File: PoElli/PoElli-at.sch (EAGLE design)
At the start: 49 parts, among them J1 DF12-60DP, T1 POE-ISOLATION, U3 NCP1117, X1 RJ45MOLEX

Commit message: Added ENC624J600
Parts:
- removed U4: (no value), SparkFun-DigitalIC:ENC28J60
- added C11, C14: 10n, ELL-i-Passives:C0603
- added C12, C13: 6.8n, ELL-i-Passives:C0603
- added C15: 10u, ELL-i-Passives:C0603
- added C16: 47u, ELL-i-Passives:CPOL6032
- added C17: 100n, ELL-i-Passives:C0805
- added C18, C19: 27p, ELL-i-Passives:C0603
- added D11: GREEN, SparkFun-LED:LED-GREEN0603
- added D12: (no value), SparkFun-LED:LED-YELLOW0603
- added R16, R17: 180, ELL-i-Passives:R0402
- added R18, R20: 49.9,1%, ELL-i-Passives:R0603
- added R19: 10R, 1%, ELL-i-Passives:R0603
- added R21: 12.4k,1%, ELL-i-Passives:R0603
- added U$4: ENC624J600-I/PT, ELL-i-DigitalIC:ENC624J600-I/PT
- R1, R2: value 100 -> 49.9,1%
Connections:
- new net +3V3: C16.+, R18.1, R19.2, R2.2, U$4.VDD, U$4.VDDOSC, U$4.VDDPLL, U$4.VDDRX, U$4.VDDTX, U$4.VDD_2, U$4.VDD_3, U3.OUT, U3.TAB
- new net GNDA: C10.-, C11.2, C14.2, C15.2, C16.-, C17.2, C18.2, C19.2, D11.C, D12.C, R15.1, R21.1, U$4.A0, U$4.A1, U$4.A10, U$4.A11, U$4.A12, U$4.A13, U$4.A14/PSPCFG1, U$4.A2, U$4.A3, U$4.A4, U$4.A5, U$4.A6, U$4.A7, U$4.A8, U$4.A9, U$4.AD0, U$4.AD1, U$4.AD10, U$4.AD11, U$4.AD12, U$4.AD13, U$4.AD14, U$4.AD15, U$4.AD2, U$4.AD3, U$4.AD4, U$4.AD5, U$4.AD6, U$4.AD7, U$4.AD8, U$4.AD9, U$4.PSPCFG2, U$4.PSPCFG3, U$4.VSS, U$4.VSSOSC, U$4.VSSPLL, U$4.VSSRX, U$4.VSSTX, U$4.VSSTX1, U$4.VSS_2, U$4.WRH/B1SEL, U$7.SEC-, U3.GND
- new net N$38: D11.A, R17.1
- new net N$39: C12.1, T1.RD+
- new net N$40: C12.2, R1.1, U$4.TPIN-
- new net N$41: R16.1, U$4.LEDB
- new net N$42: R17.2, U$4.LEDA
- new net N$43: C11.1, R19.1, T1.TCT
- new net N$44: C13.2, R20.2, U$4.TPIN+
- new net N$45: R21.2, U$4.RBIAS
- new net N$46: C15.1, U$4.VCAP
- new net N$47: C19.1, U$4.OSC1
- net N$11: now also C14.1, R20.1, T1.RCT; no longer T1.RD-
- net N$12: now also C13.1, T1.RD-; no longer R1.1, T1.RD+
- net N$13: now also R18.2, U$4.TPOUT+; no longer R2.2
- net N$14: now also U$4.TPOUT-
- net N$35: now also C17.1
- net N$36: now also D12.A, R16.2; no longer C10.-, R15.1, U$7.SEC-
- net N$37: now also C18.1, U$4.OSC2; no longer U3.OUT, U3.TAB, U4.VDD, U4.VDDOSC, U4.VDDPLL, U4.VDDRX, U4.VDDTX
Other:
- moved on the sheet: J1, R1, R2, SV1, T1, U3, X1

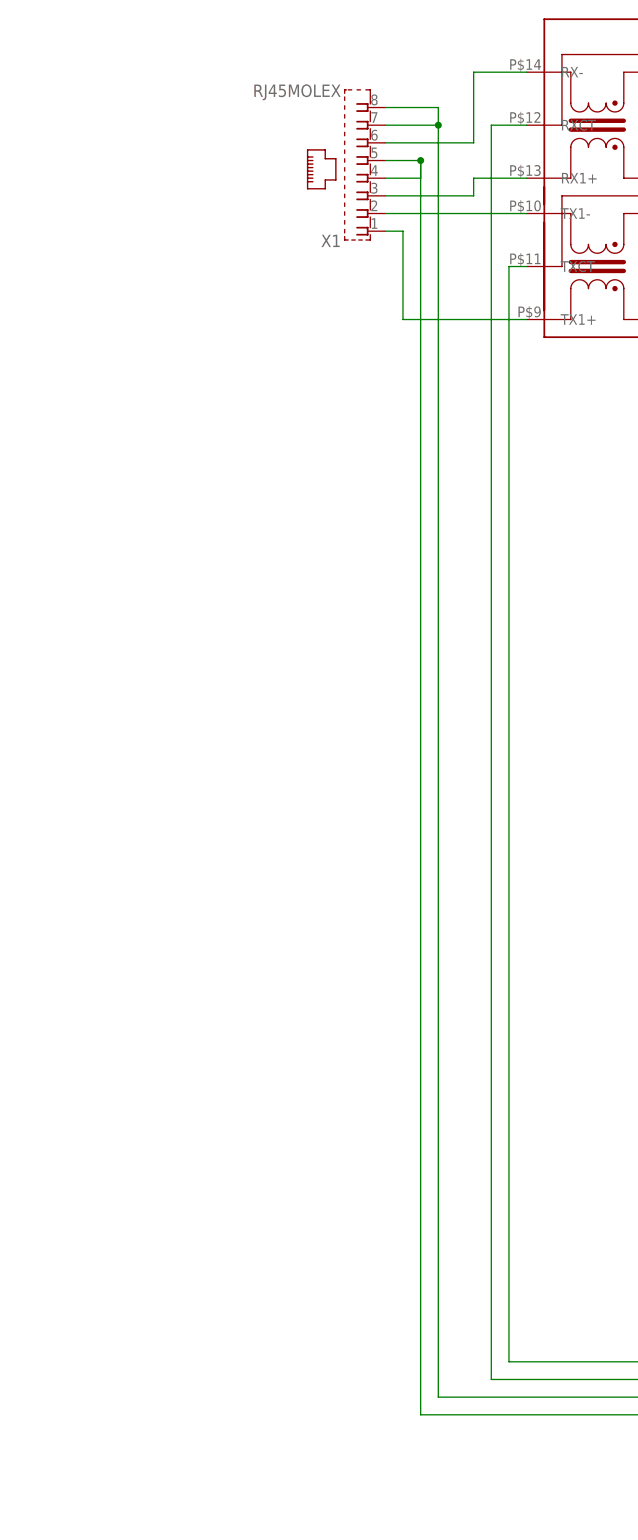
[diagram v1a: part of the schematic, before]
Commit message: Added RC-snubber to bridge rectifier
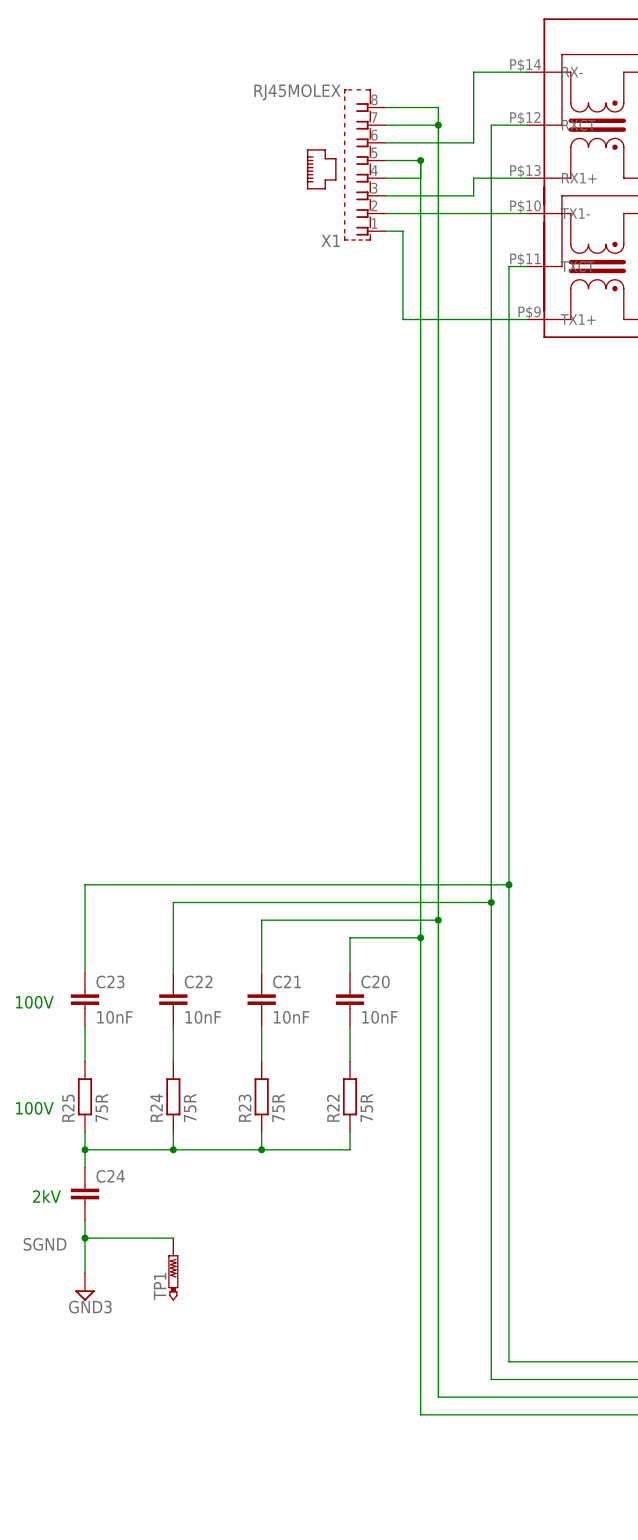
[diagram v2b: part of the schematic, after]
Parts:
- added C20, C21, C22, C23: 10nF, ELL-i-Passives:C0805
- added C24: (no value), ELL-i-Passives:C0805
- added R22, R23, R24, R25: 75R, ELL-i-Passives:R0805
- added TP1: PTR1B2,54, testpad:PTR1B2,54
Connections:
- new net N$48: C20.2, R22.2
- new net N$49: C24.1, R22.1, R23.1, R24.1, R25.1
- new net N$50: C23.2, R25.2
- new net N$51: C22.2, R24.2
- new net N$52: C21.2, R23.2
- new net SGND: C24.2, TP1.TP
- net N$10: now also C23.1
- net N$5: now also C21.1
- net N$7: now also C20.1
- net N$9: now also C22.1
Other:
- note added: "100V"
- note added: "2kV"
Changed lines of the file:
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@@
 <part name="GND15" library="supply1" deviceset="GNDA" device=""/>
 <part name="GND16" library="supply1" deviceset="GNDA" device=""/>
+<part name="R22" library="ELL-i-Passives" deviceset="R" device="0805" value="75R"/>
+<part name="R23" library="ELL-i-Passives" deviceset="R" device="0805" value="75R"/>
+<part name="R24" library="ELL-i-Passives" deviceset="R" device="0805" value="75R"/>
+<part name="R25" library="ELL-i-Passives" deviceset="R" device="0805" value="75R"/>
+<part name="C20" library="ELL-i-Passives" deviceset="C" device="0805" value="10nF"/>
+<part name="C21" library="ELL-i-Passives" deviceset="C" device="0805" value="10nF"/>
+<part name="C22" library="ELL-i-Passives" deviceset="C" device="0805" value="10nF"/>
+<part name="C23" library="ELL-i-Passives" deviceset="C" device="0805" value="10nF"/>
+<part name="C24" library="ELL-i-Passives" deviceset="C" device="0805"/>
+<part name="TP1" library="testpad" deviceset="PTR1" device="B2,54"/>
+<part name="SUPPLY1" library="supply2" deviceset="GND3" device=""/>
 </parts>
 <sheets>
 <sheet>
 <plain>
+<text x="-132.08" y="91.44" size="1.778" layer="91">2kV</text>
+<text x="-134.62" y="119.38" size="1.778" layer="91">100V</text>
+<text x="-134.62" y="104.14" size="1.778" layer="91">100V</text>
 </plain>
 <instances>
@@
 <instance part="GND15" gate="1" x="157.48" y="208.28"/>
 <instance part="GND16" gate="1" x="172.72" y="208.28"/>
+<instance part="R22" gate="G$1" x="-86.36" y="106.68" rot="R90"/>
+<instance part="R23" gate="G$1" x="-99.06" y="106.68" rot="R90"/>
+<instance part="R24" gate="G$1" x="-111.76" y="106.68" rot="R90"/>
+<instance part="R25" gate="G$1" x="-124.46" y="106.68" rot="R90"/>
+<instance part="C20" gate="G$1" x="-86.36" y="121.92"/>
+<instance part="C21" gate="G$1" x="-99.06" y="121.92"/>
+<instance part="C22" gate="G$1" x="-111.76" y="121.92"/>
+<instance part="C23" gate="G$1" x="-124.46" y="121.92"/>
+<instance part="C24" gate="G$1" x="-124.46" y="93.98"/>
+<instance part="TP1" gate="G$1" x="-111.76" y="83.82"/>
+<instance part="SUPPLY1" gate="G$1" x="-124.46" y="78.74"/>
 </instances>
 <busses>
@@
 <wire x1="-81.28" y1="248.92" x2="-73.66" y2="248.92" width="0.1524" layer="91"/>
 <wire x1="-73.66" y1="248.92" x2="-73.66" y2="246.38" width="0.1524" layer="91"/>
-<wire x1="-73.66" y1="246.38" x2="-73.66" y2="63.5" width="0.1524" layer="91"/>
+<wire x1="-73.66" y1="246.38" x2="-73.66" y2="132.08" width="0.1524" layer="91"/>
 <pinref part="X1" gate="G$1" pin="7"/>
+<wire x1="-73.66" y1="132.08" x2="-73.66" y2="63.5" width="0.1524" layer="91"/>
 <wire x1="-81.28" y1="246.38" x2="-73.66" y2="246.38" width="0.1524" layer="91"/>
 <junction x="-73.66" y="246.38"/>
@@
 <wire x1="-5.08" y1="63.5" x2="-73.66" y2="63.5" width="0.1524" layer="91"/>
 <junction x="-5.08" y="63.5"/>
+<pinref part="C21" gate="G$1" pin="1"/>
+<wire x1="-99.06" y1="124.46" x2="-99.06" y2="132.08" width="0.1524" layer="91"/>
+<wire x1="-99.06" y1="132.08" x2="-73.66" y2="132.08" width="0.1524" layer="91"/>
+<junction x="-73.66" y="132.08"/>
 </segment>
 </net>
@@
 <wire x1="-15.24" y1="68.58" x2="-15.24" y2="43.18" width="0.1524" layer="91"/>
 <wire x1="-60.96" y1="226.06" x2="-63.5" y2="226.06" width="0.1524" layer="91"/>
-<wire x1="-63.5" y1="226.06" x2="-63.5" y2="68.58" width="0.1524" layer="91"/>
+<wire x1="-63.5" y1="226.06" x2="-63.5" y2="137.16" width="0.1524" layer="91"/>
+<junction x="-15.24" y="68.58"/>
+<wire x1="-63.5" y1="137.16" x2="-63.5" y2="68.58" width="0.1524" layer="91"/>
 <wire x1="-15.24" y1="68.58" x2="-63.5" y2="68.58" width="0.1524" layer="91"/>
-<junction x="-15.24" y="68.58"/>
+<pinref part="C23" gate="G$1" pin="1"/>
+<wire x1="-124.46" y1="124.46" x2="-124.46" y2="137.16" width="0.1524" layer="91"/>
+<wire x1="-124.46" y1="137.16" x2="-63.5" y2="137.16" width="0.1524" layer="91"/>
+<junction x="-63.5" y="137.16"/>
 </segment>
 </net>
@@
 <wire x1="-10.16" y1="66.04" x2="-10.16" y2="43.18" width="0.1524" layer="91"/>
 <wire x1="-60.96" y1="246.38" x2="-66.04" y2="246.38" width="0.1524" layer="91"/>
-<wire x1="-66.04" y1="246.38" x2="-66.04" y2="66.04" width="0.1524" layer="91"/>
+<wire x1="-66.04" y1="246.38" x2="-66.04" y2="134.62" width="0.1524" layer="91"/>
+<wire x1="-66.04" y1="134.62" x2="-66.04" y2="66.04" width="0.1524" layer="91"/>
 <wire x1="-10.16" y1="66.04" x2="-66.04" y2="66.04" width="0.1524" layer="91"/>
 <junction x="-10.16" y="66.04"/>
+<pinref part="C22" gate="G$1" pin="1"/>
+<wire x1="-111.76" y1="124.46" x2="-111.76" y2="134.62" width="0.1524" layer="91"/>
+<wire x1="-111.76" y1="134.62" x2="-66.04" y2="134.62" width="0.1524" layer="91"/>
+<junction x="-66.04" y="134.62"/>
 </segment>
 </net>
@@
 <pinref part="X1" gate="G$1" pin="5"/>
 <wire x1="-81.28" y1="241.3" x2="-76.2" y2="241.3" width="0.1524" layer="91"/>
-<wire x1="-76.2" y1="241.3" x2="-76.2" y2="60.96" width="0.1524" layer="91"/>
+<wire x1="-76.2" y1="241.3" x2="-76.2" y2="129.54" width="0.1524" layer="91"/>
 <pinref part="X1" gate="G$1" pin="4"/>
+<wire x1="-76.2" y1="129.54" x2="-76.2" y2="60.96" width="0.1524" layer="91"/>
 <wire x1="-81.28" y1="238.76" x2="-76.2" y2="238.76" width="0.1524" layer="91"/>
 <wire x1="-76.2" y1="238.76" x2="-76.2" y2="241.3" width="0.1524" layer="91"/>
 <junction x="-76.2" y="241.3"/>
+<pinref part="C20" gate="G$1" pin="1"/>
+<wire x1="-86.36" y1="124.46" x2="-86.36" y2="129.54" width="0.1524" layer="91"/>
+<wire x1="-86.36" y1="129.54" x2="-76.2" y2="129.54" width="0.1524" layer="91"/>
+<junction x="-76.2" y="129.54"/>
 </segment>
 </net>
@@
 </segment>
 </net>
+<net name="N$49" class="0">
+<segment>
+<pinref part="C24" gate="G$1" pin="1"/>
+<wire x1="-124.46" y1="99.06" x2="-124.46" y2="96.52" width="0.1524" layer="91"/>
+<wire x1="-86.36" y1="99.06" x2="-99.06" y2="99.06" width="0.1524" layer="91"/>
+<pinref part="R25" gate="G$1" pin="1"/>
+<wire x1="-99.06" y1="99.06" x2="-111.76" y2="99.06" width="0.1524" layer="91"/>
+<wire x1="-111.76" y1="99.06" x2="-124.46" y2="99.06" width="0.1524" layer="91"/>
+<wire x1="-124.46" y1="99.06" x2="-124.46" y2="101.6" width="0.1524" layer="91"/>
+<pinref part="R24" gate="G$1" pin="1"/>
+<wire x1="-111.76" y1="101.6" x2="-111.76" y2="99.06" width="0.1524" layer="91"/>
+<pinref part="R23" gate="G$1" pin="1"/>
+<wire x1="-99.06" y1="101.6" x2="-99.06" y2="99.06" width="0.1524" layer="91"/>
+<pinref part="R22" gate="G$1" pin="1"/>
+<wire x1="-86.36" y1="101.6" x2="-86.36" y2="99.06" width="0.1524" layer="91"/>
+<junction x="-124.46" y="99.06"/>
+<junction x="-111.76" y="99.06"/>
+<junction x="-99.06" y="99.06"/>
+</segment>
+</net>
+<net name="SGND" class="0">
+<segment>
+<pinref part="SUPPLY1" gate="G$1" pin="GND3"/>
+<pinref part="C24" gate="G$1" pin="2"/>
+<wire x1="-124.46" y1="81.28" x2="-124.46" y2="86.36" width="0.1524" layer="91"/>
+<pinref part="TP1" gate="G$1" pin="TP"/>
+<wire x1="-124.46" y1="86.36" x2="-124.46" y2="88.9" width="0.1524" layer="91"/>
+<wire x1="-111.76" y1="86.36" x2="-124.46" y2="86.36" width="0.1524" layer="91"/>
+<junction x="-124.46" y="86.36"/>
+<label x="-127" y="86.36" size="1.778" layer="95" rot="R180"/>
+</segment>
+</net>
+<net name="N$48" class="0">
+<segment>
+<pinref part="R22" gate="G$1" pin="2"/>
+<pinref part="C20" gate="G$1" pin="2"/>
+<wire x1="-86.36" y1="111.76" x2="-86.36" y2="116.84" width="0.1524" layer="91"/>
+</segment>
+</net>
+<net name="N$50" class="0">
+<segment>
+<pinref part="C23" gate="G$1" pin="2"/>
+<pinref part="R25" gate="G$1" pin="2"/>
+<wire x1="-124.46" y1="116.84" x2="-124.46" y2="111.76" width="0.1524" layer="91"/>
+</segment>
+</net>
+<net name="N$51" class="0">
+<segment>
+<pinref part="R24" gate="G$1" pin="2"/>
+<pinref part="C22" gate="G$1" pin="2"/>
+<wire x1="-111.76" y1="111.76" x2="-111.76" y2="116.84" width="0.1524" layer="91"/>
+</segment>
+</net>
+<net name="N$52" class="0">
+<segment>
+<pinref part="C21" gate="G$1" pin="2"/>
+<pinref part="R23" gate="G$1" pin="2"/>
+<wire x1="-99.06" y1="116.84" x2="-99.06" y2="111.76" width="0.1524" layer="91"/>
+</segment>
+</net>

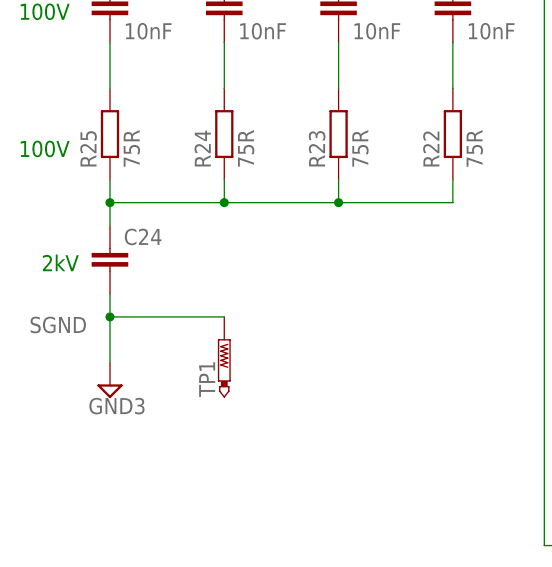
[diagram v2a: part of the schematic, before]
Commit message: Added RC-snubber value
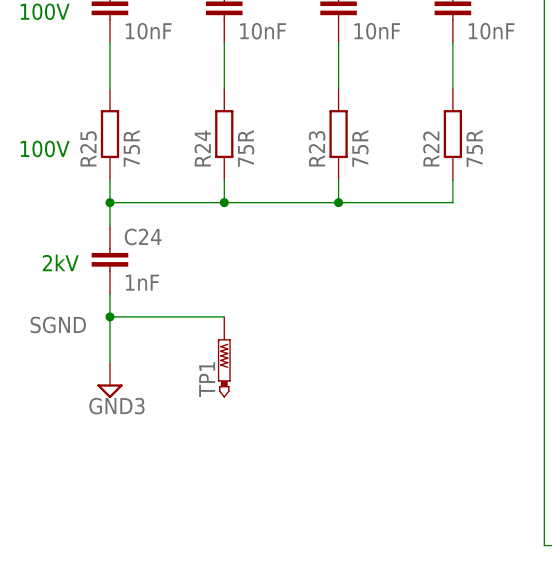
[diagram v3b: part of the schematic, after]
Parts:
- C24: value (none) -> 1nF
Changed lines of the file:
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@@
 <part name="C22" library="ELL-i-Passives" deviceset="C" device="0805" value="10nF"/>
 <part name="C23" library="ELL-i-Passives" deviceset="C" device="0805" value="10nF"/>
-<part name="C24" library="ELL-i-Passives" deviceset="C" device="0805"/>
+<part name="C24" library="ELL-i-Passives" deviceset="C" device="0805" value="1nF"/>
 <part name="TP1" library="testpad" deviceset="PTR1" device="B2,54"/>
 <part name="SUPPLY1" library="supply2" deviceset="GND3" device=""/>

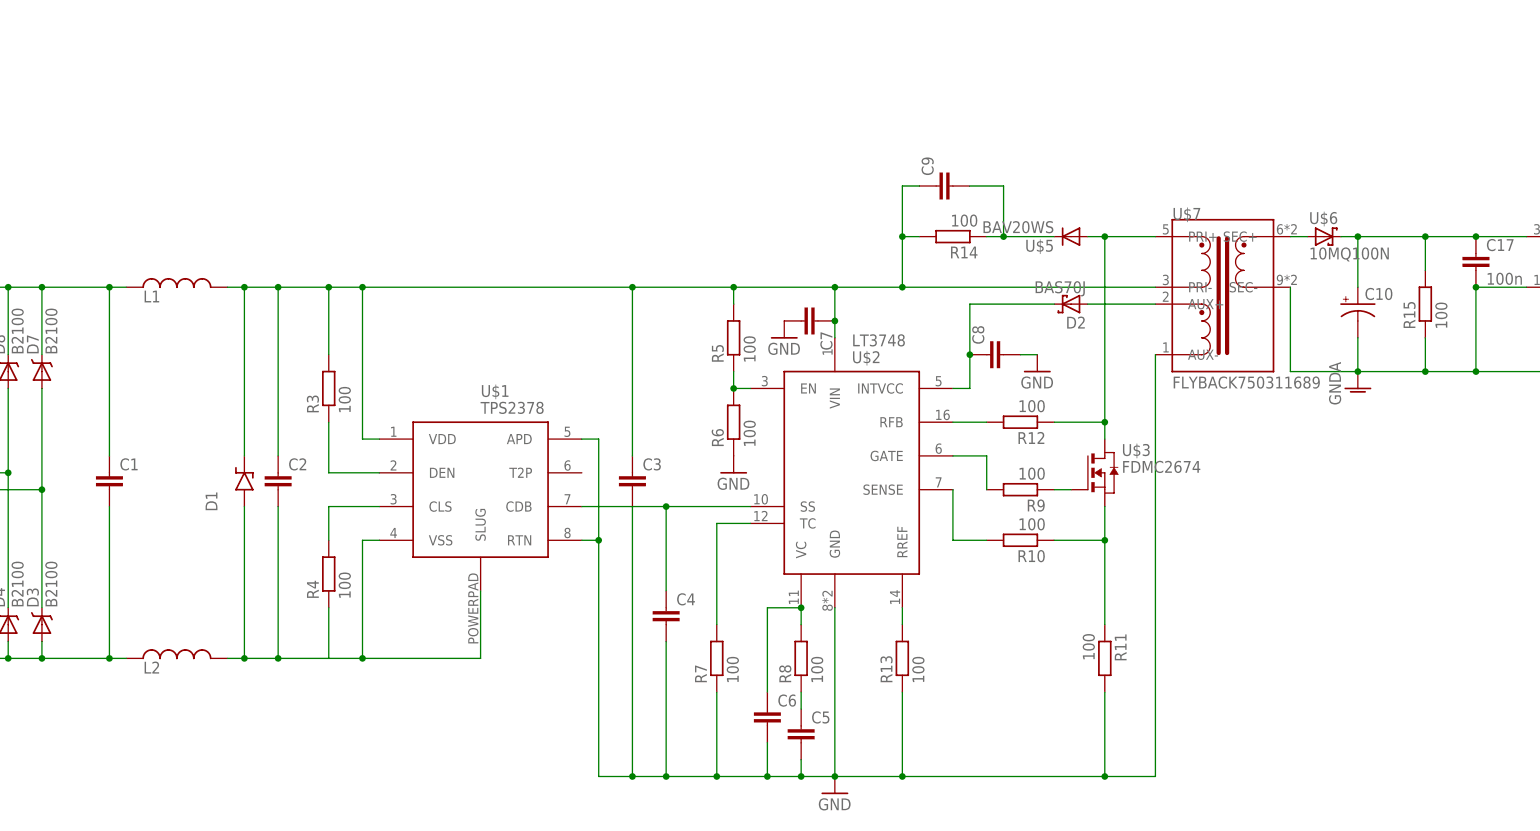
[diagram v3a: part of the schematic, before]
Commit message: Added component values around flyback
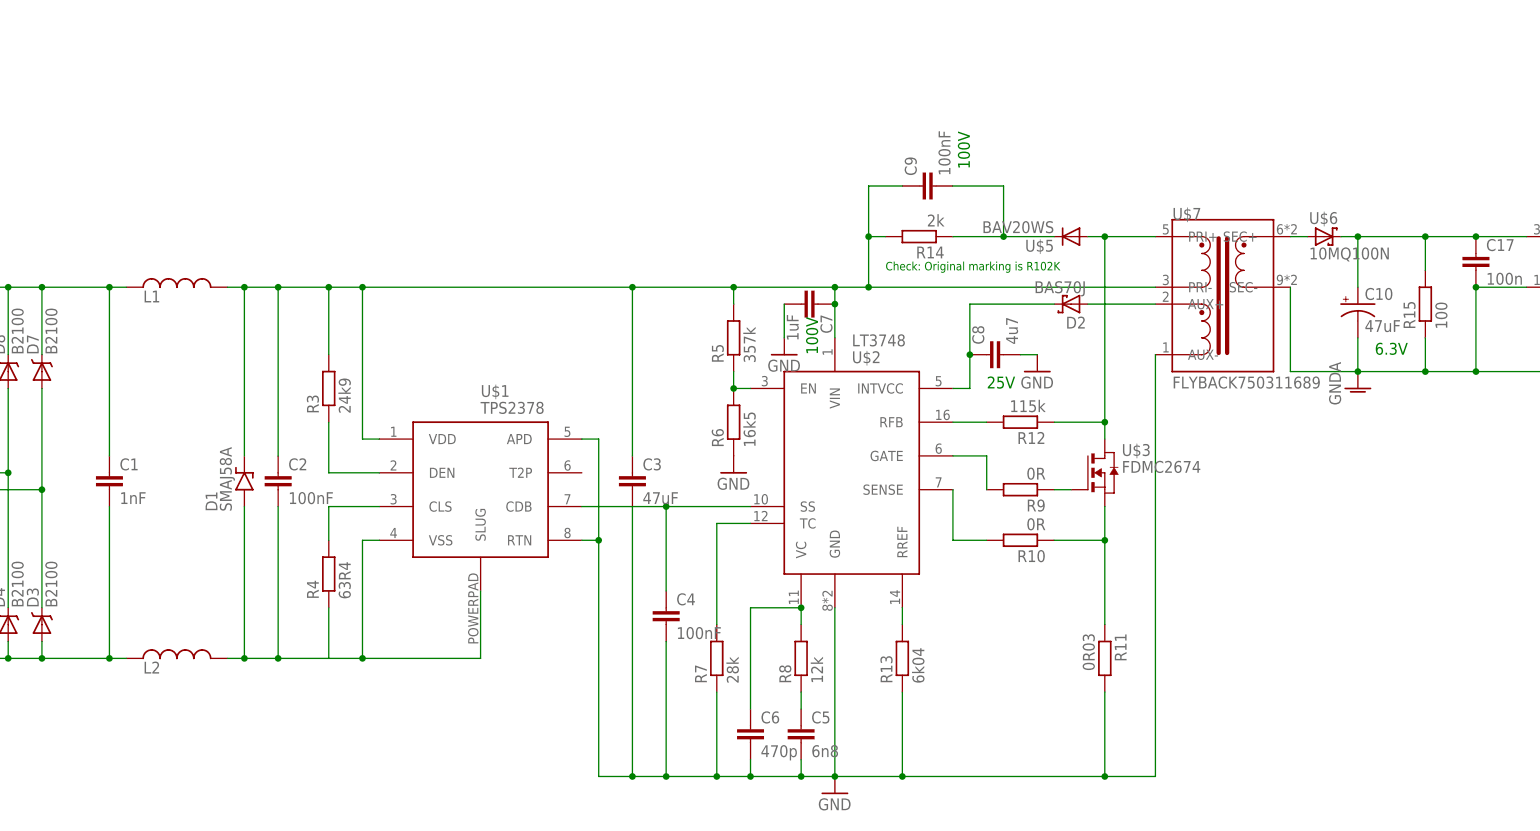
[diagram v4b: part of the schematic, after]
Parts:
- C1: value (none) -> 1nF
- C10, C3: value (none) -> 47uF
- C2, C4, C9: value (none) -> 100nF
- C5: value (none) -> 6n8
- C6: value (none) -> 470p
- C7: value (none) -> 1uF
- C8: value (none) -> 4u7
- D1: value (none) -> SMAJ58A
- R10, R9: value 100 -> 0R
- R11: value 100 -> 0R03
- R12: value 100 -> 115k
- R13: value 100 -> 6k04
- R14: value 100 -> 2k
- R3: value 100 -> 24k9
- R4: value 100 -> 63R4
- R5: value 100 -> 357k
- R6: value 100 -> 16k5
- R7: value 100 -> 28k
- R8: value 100 -> 12k
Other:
- note added: "25V"
- note added: "6.3V"
- note added: "Check: Original marking is R102K"
- moved on the sheet: C6, C7, C9, R14
